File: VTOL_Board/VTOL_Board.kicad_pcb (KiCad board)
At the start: 2 copper layers, 157 x 47 mm, 65 parts, among them J101 MOTOR, J102 ENCODER, J201 ICSP, J302 19V Input, J401 USB_B_Micro, J402 PROG, Q101 MMBT3904, Q102 MMBT3906, SW201 RESET, SW202 START_SW, SW203 STOP/MODE_SW, U201 ATmega328P, U301 NCV1117ST50T3G, U401 FT232RL, Y201 16mHz

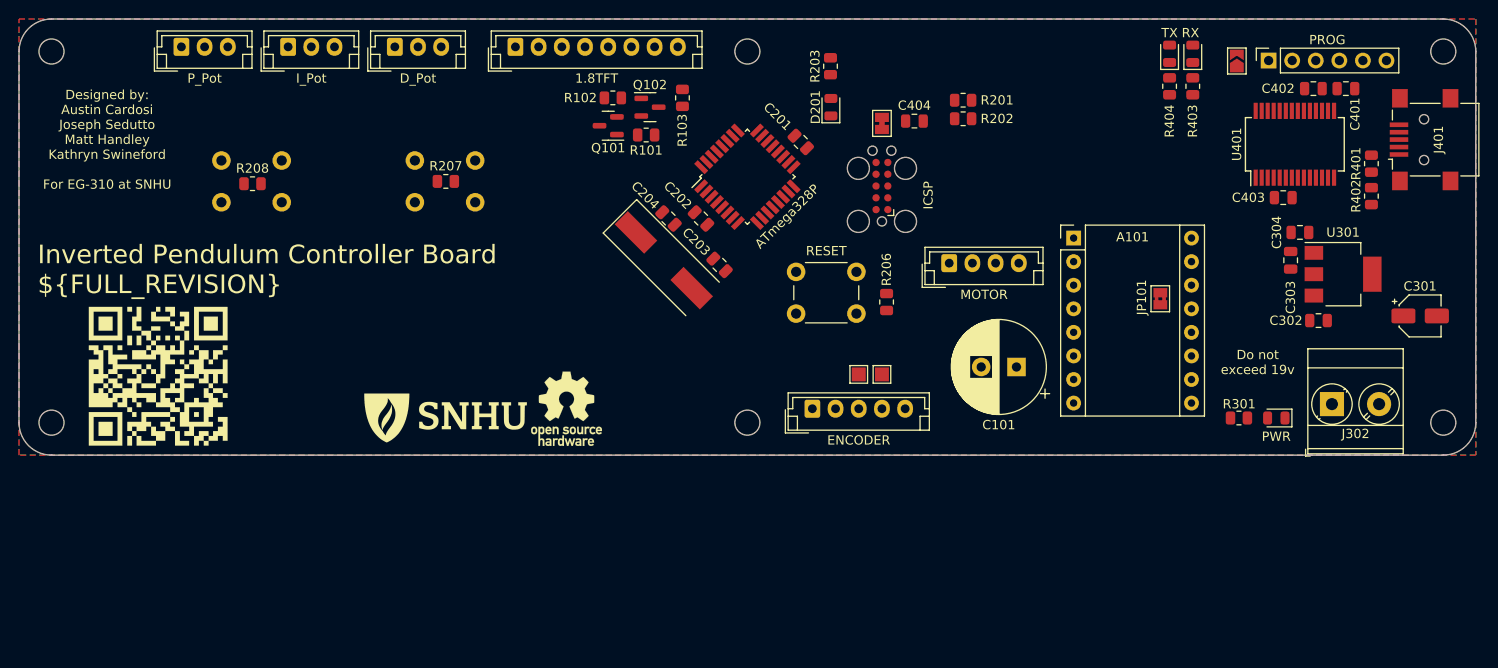
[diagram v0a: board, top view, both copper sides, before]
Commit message: Use small hirose connectors
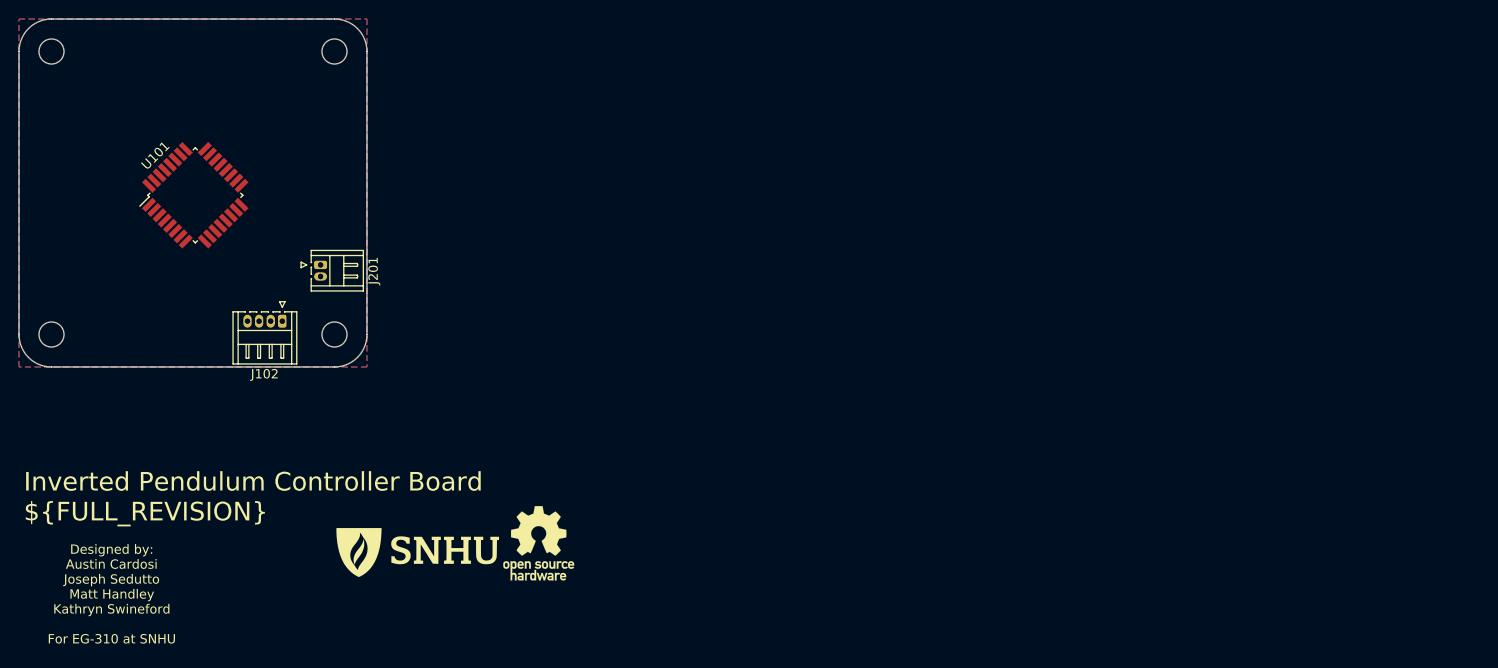
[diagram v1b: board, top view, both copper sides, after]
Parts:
- removed A101: A4988, Module:Pololu_Breakout-16_15.2x20.3mm
- removed C101: 10uf, Capacitor_THT:CP_Radial_D10.0mm_P3.80mm
- removed C201, C202: 100nf, Capacitor_SMD:C_0805_2012Metric
- removed C203, C204: 22pf, Capacitor_SMD:C_0805_2012Metric
- removed C301: 10uf, Capacitor_SMD:CP_Elec_4x3
- removed C302, C303, C401, C402, C403, C404: 100nF, Capacitor_SMD:C_0805_2012Metric
- removed C304: 1uF, Capacitor_SMD:C_0805_2012Metric
- removed D101: 1.8TFT, Connector_JST:JST_EH_B8B-EH-A_1x08_P2.50mm_Vertical
- removed D201: STAT, LED_SMD:LED_0805_2012Metric
- removed D301: PWR, LED_SMD:LED_0805_2012Metric
- removed D401: RX, LED_SMD:LED_0805_2012Metric
- removed D402: TX, LED_SMD:LED_0805_2012Metric
- removed H101, H104: PiMountingHole, MountingHole:MountingHole_2.7mm
- removed J101: MOTOR, Connector_JST:JST_EH_B4B-EH-A_1x04_P2.50mm_Vertical
- removed J302: 19V Input, TerminalBlock_Phoenix:TerminalBlock_Phoenix_MKDS-3-2-5.08_1x02_P5.08mm_Horizontal
- removed J401: USB_B_Micro, Connector_USB:USB_Mini-B_Lumberg_2486_01_Horizontal
- removed J402: PROG, Connector_PinSocket_2.54mm:PinSocket_1x06_P2.54mm_Vertical
- removed JP101: SolderJumper_2_Bridged, Jumper:SolderJumper-2_P1.3mm_Bridged2Bar_Pad1.0x1.5mm
- removed JP201: RSTBridge, Jumper:SolderJumper-2_P1.3mm_Bridged_Pad1.0x1.5mm
- removed JP401: SolderJumper_2_Open, Jumper:SolderJumper-2_P1.3mm_Open_TrianglePad1.0x1.5mm
- removed Q101: MMBT3904, Package_TO_SOT_SMD:SOT-23
- removed Q102: MMBT3906, Package_TO_SOT_SMD:SOT-23
- removed QRCODE: LOGO, Misc:custom_silkscreen
- removed R101, R207, R208, R402: 10K, Resistor_SMD:R_0805_2012Metric
- removed R102: 2K2, Resistor_SMD:R_0805_2012Metric
- removed R103: TBD, Resistor_SMD:R_0805_2012Metric
- removed R201, R202, R203, R206, R301, R403, R404: 1K, Resistor_SMD:R_0805_2012Metric
- removed R401: 4K7, Resistor_SMD:R_0805_2012Metric
- removed RV201: P_Pot, Connector_JST:JST_EH_B3B-EH-A_1x03_P2.50mm_Vertical
- removed RV202: I_Pot, Connector_JST:JST_EH_B3B-EH-A_1x03_P2.50mm_Vertical
- removed RV203: D_Pot, Connector_JST:JST_EH_B3B-EH-A_1x03_P2.50mm_Vertical
- removed SW201: RESET, Button_Switch_THT:SW_PUSH_6mm_H5mm
- removed SW202: START_SW, Button_Switch_THT:SW_PUSH_6mm_H5mm
- removed SW203: STOP/MODE_SW, Button_Switch_THT:SW_PUSH_6mm_H5mm
- removed TP101, TP102: TestPoint, TestPoint:TestPoint_Pad_1.5x1.5mm
- removed U201: ATmega328P, Package_QFP:TQFP-32_7x7mm_P0.8mm
- removed U301: NCV1117ST50T3G, Package_TO_SOT_SMD:SOT-223
- removed U401: FT232RL, Package_SO:SSOP-28_5.3x10.2mm_P0.65mm
- removed Y201: 16mHz, Crystal:Crystal_SMD_HC49-SD
- added U101: ATmega328P, Package_QFP:TQFP-32_7x7mm_P0.8mm, F.Cu at (85.5, 85.5)
- J102: value ENCODER -> Servo1; footprint Connector_JST:JST_EH_B5B-EH-A_1x05_P2.50mm_Vertical -> Connector_Hirose:Hirose_DF13-04P-1.25DS_1x04_P1.25mm_Horizontal
- J201: value ICSP -> PWR In; footprint Connector:Tag-Connect_TC2050-IDC-FP_2x05_P1.27mm_Vertical -> Connector_Hirose:Hirose_DF13-02P-1.25DS_1x02_P1.25mm_Horizontal
- moved J201 61.1 mm to (99.0, 93.0), turned to -90 degrees
- moved J102 57.9 mm to (94.9, 99.1), turned to 180 degrees
- moved H102 45.5 mm to (100.5, 100.5)
- moved H103 44.5 mm to (100.5, 70.0)
- moved REF** 14.8 mm to (122.5, 123.0)
- moved SNHU_NEW*** 14.8 mm to (109.5, 124.0)
- moved H106 9.50 mm to (70.0, 100.5)
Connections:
- J102 pad 1: GND -> unconnected-(J102-Pad1)
- J102 pad 2: GND -> unconnected-(J102-Pad2)
- J102 pad 3: /EncA -> unconnected-(J102-Pad3)
- J102 pad 4: /EncB -> unconnected-(J102-Pad4)
- J201 pad 1: /MCU/SDO -> +19V
- J201 pad 2: +5V -> GND
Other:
- board size 157 x 47 mm -> 37.5 x 37.5 mm
- board text removed: "Do not exceed 19v"
